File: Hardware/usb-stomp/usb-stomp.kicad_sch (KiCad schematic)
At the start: 30 parts, among them J1 Conn_01x12_MountingPin, J2 USB_C_Receptacle_USB2.0_16P, J3 BM28B0.6-24DS/2, J4 AudioJack4, J5 AudioJack4, J6 I2C1, SW1 SW_SPST, U1 TLV76733DRVx, U2 USBLC6-2P6, U3 74AHCT1G125, U4 TLP2310

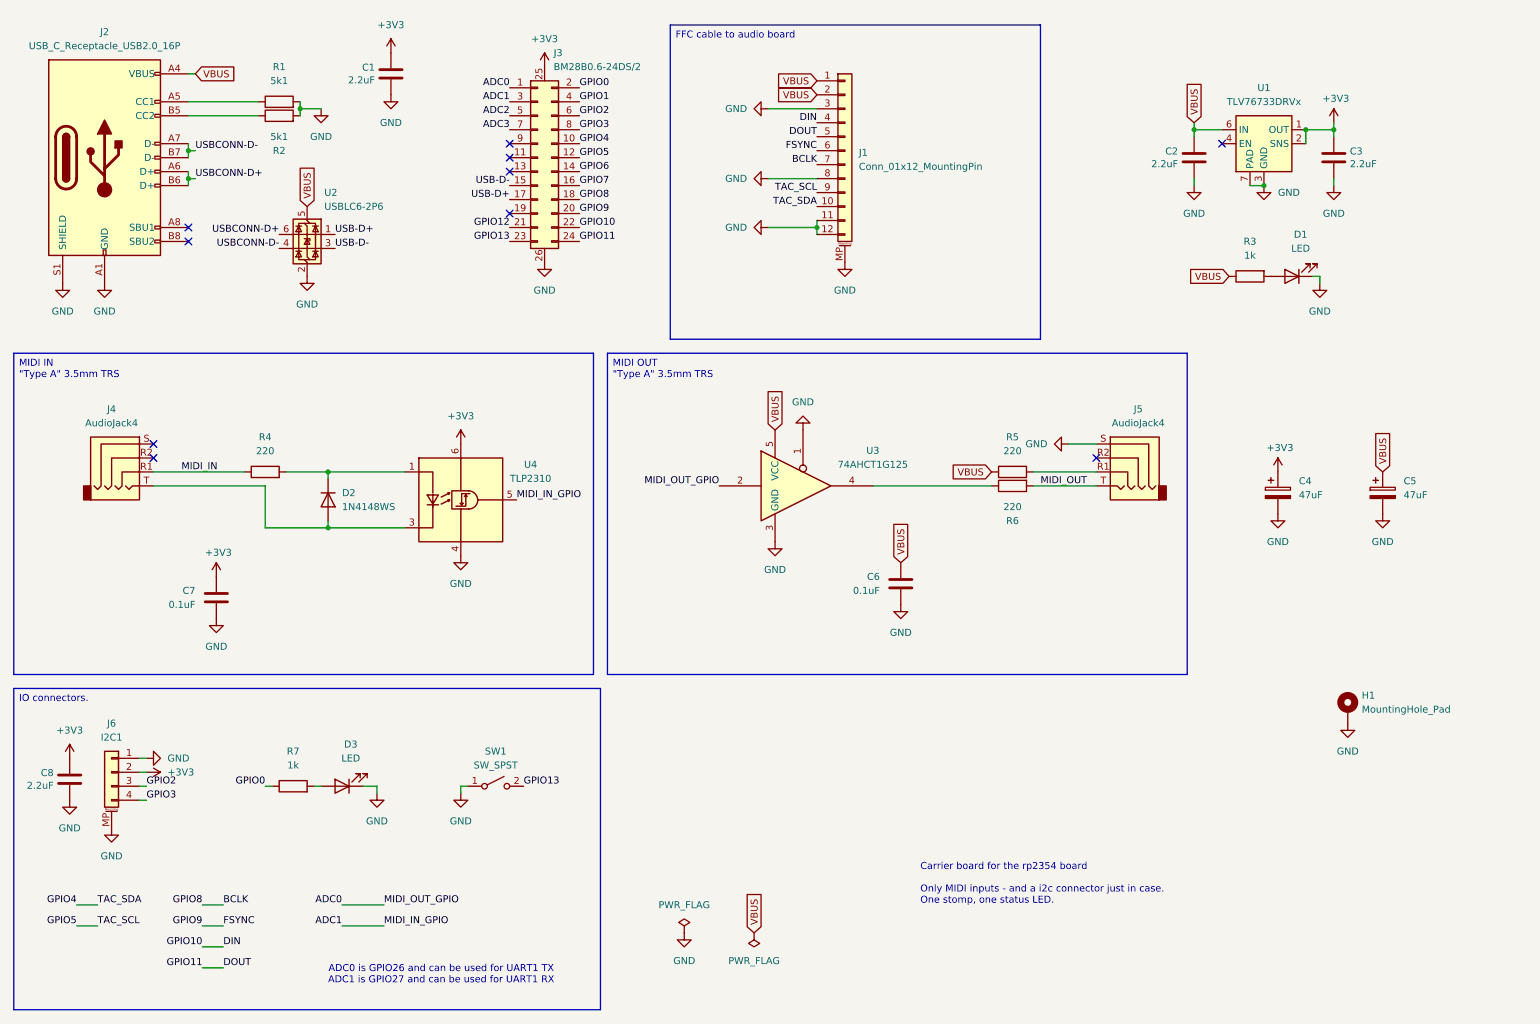
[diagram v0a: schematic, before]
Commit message: Update the "USB Stomp" board to use design blocks
This is pretty much a re-do of the "USB Stomp" board to include
everything into one single design and one single resulting board.

It makes little sense - it's not that interesting a board - but the
impetus was mostly just to learn and use new features, both on the
design side and on the manufacturing side.

So this does two very big things:

 - it uses the new TAC5242 / RP2354 design blocks as part of the
   schematic and the PCB layout.

 - the board is manufactured as one single flex board instead of having
   separate "audio jacks" and "USB stomp" boards

In other words, it's the same as the combination of the "audio jacks"
board and the previous "USB stomp" board, that used a FFC cable to
connect the two, except now the FFC cable is basically part of the
design, and the traditional rigid parts have been replaced by FR4
stiffeners instead.

In the process, this does various other minor changes:

 - No more separate BOOTSEL switch, which was a nightmare when the thing
   was boxed up. Instead, the stomp switch doubles up as the BOOTSEL
   switch too.

   Connecting the same switch to both a GPIO and BOOTSEL needs a bit of
   care: it would have been technically possible to only connect it to
   the the BOOTSEL pin, and read it that way with no GPIO at all, but
   the BOOTSEL line is also tied to the QSPI chip select pin, so then
   reading just the status requires turning off FLASH access.

   I considered doing exactly that, and it is entirely possible to do
   (micropython even has a "rp2.bootsel_button()" function for this),
   but when you use both cores, it's just very painful to make sure
   neither core is accessing the flash while you read the BOOTSEL
   status.

   So adding a little bit of hardware makes it much easier, and isolates
   the GPIO from the QSPI chip select using a dual diode. The switch
   pulls both low, but the wiggling of the QSPI CS line doesn't affect
   the GPIO.

   While at it, this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
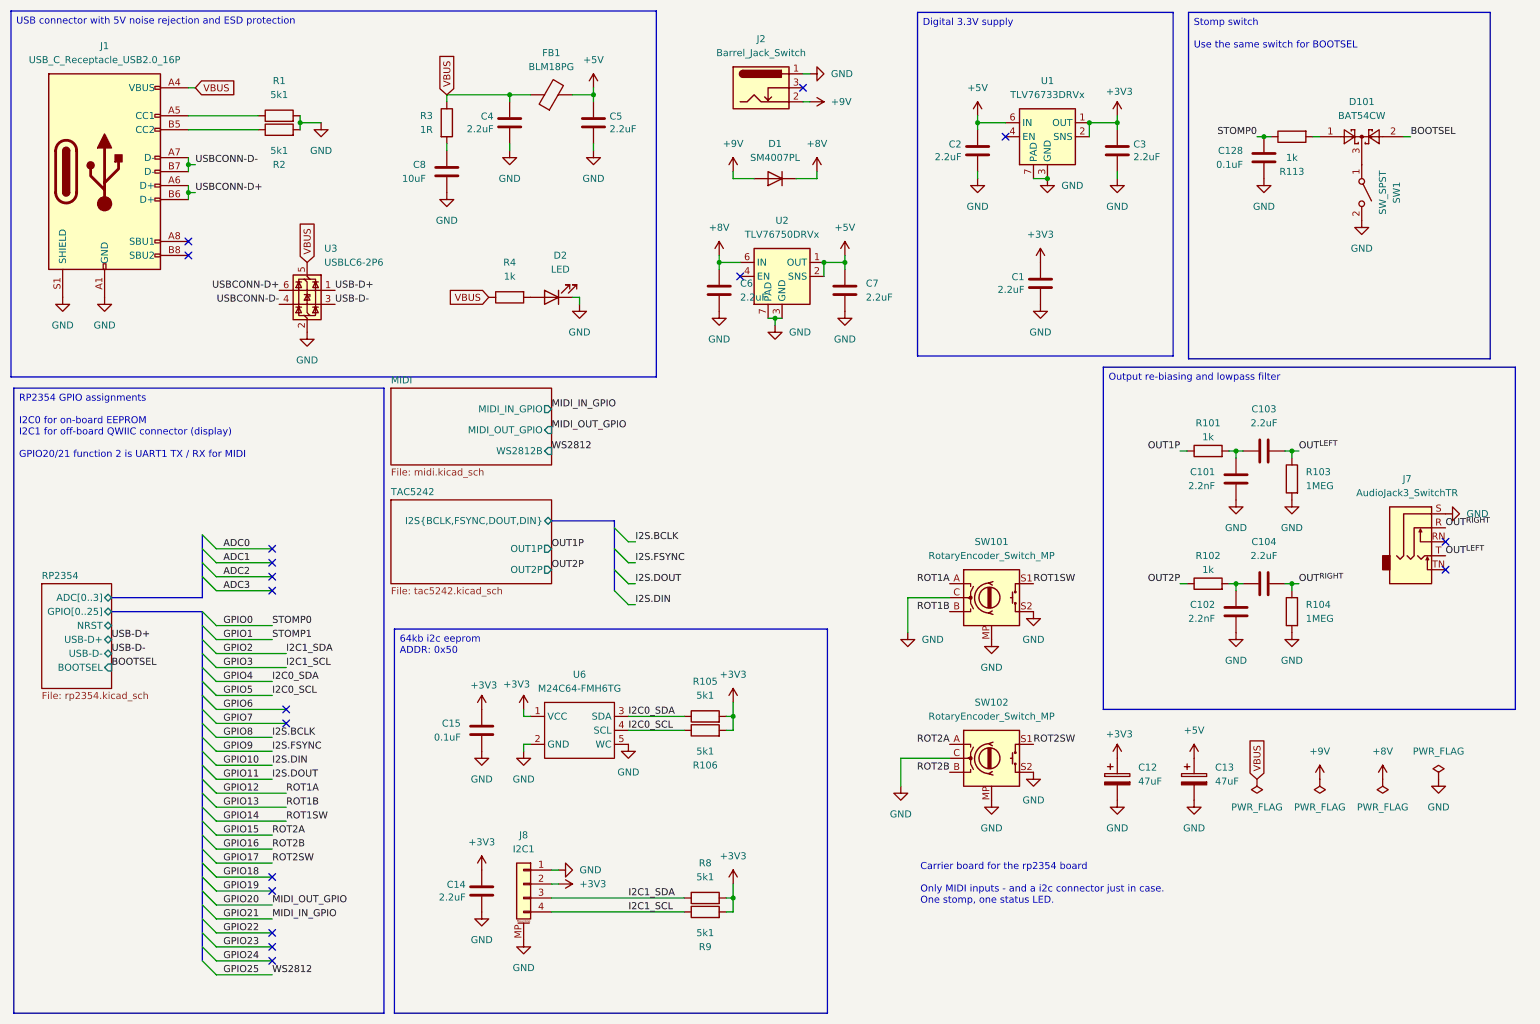
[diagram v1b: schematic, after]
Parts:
- removed D2: 1N4148WS, Diode_SMD:D_SOD-323, symbol Device:D
- removed D3: LED, LED_THT:LED_D5.0mm_FlatTop, symbol Device:LED
- removed H1: MountingHole_Pad, MountingHole:MountingHole_3.2mm_M3_DIN965_Pad, symbol Mechanical:MountingHole_Pad
- removed J1: Conn_01x12_MountingPin, Mylib:AFH-5-S12FIA-1H, symbol Connector_Generic_MountingPin:Conn_01x12_MountingPin
- removed J3: BM28B0.6-24DS/2, Mylib:BM28B0.6-24DS, symbol Mylib:BM28B0.6-24DS
- removed J4, J5: AudioJack4, Mylib:PJ-320D, symbol Connector_Audio:AudioJack4
- removed R4, R5, R6: 220, Resistor_SMD:R_0402_1005Metric, symbol Device:R
- removed R7: 1k, Resistor_SMD:R_0402_1005Metric, symbol Device:R
- removed U3: 74AHCT1G125, Package_TO_SOT_SMD:SOT-353_SC-70-5, symbol 74xGxx:74AHCT1G125
- removed U4: TLP2310, Package_SO:SO-5-6_4.55x3.7mm_P1.27mm, symbol Isolator:TLP2310
- added C101, C102: 2.2nF, Capacitor_SMD:C_0402_1005Metric, symbol Device:C
- added C103, C104, C4, C5: 2.2uF, Capacitor_SMD:C_0603_1608Metric, symbol Device:C
- added C128, C15: 0.1uF, Capacitor_SMD:C_0201_0603Metric, symbol Device:C
- added C8: 10uF, Capacitor_SMD:C_0603_1608Metric, symbol Device:C
- added D1: SM4007PL, Mylib:SOD-123FL, symbol Device:D
- added D101: BAT54CW, Package_TO_SOT_SMD:SOT-323_SC-70, symbol Diode:BAT54CW
- added FB1: BLM18PG, Inductor_SMD:L_0603_1608Metric, symbol Device:FerriteBead
- added J2: Barrel_Jack_Switch, Mylib:Wurth WR-DC 2.1mm Power Jack, symbol Connector:Barrel_Jack_Switch
- added J7: AudioJack3_SwitchTR, Mylib:NRJ6HM-1-PRE, symbol Connector_Audio:AudioJack3_SwitchTR
- added R101, R102, R113: 1k, Resistor_SMD:R_0402_1005Metric, symbol Device:R
- added R103, R104: 1MEG, Resistor_SMD:R_0402_1005Metric, symbol Device:R
- added R105, R106, R8, R9: 5k1, Resistor_SMD:R_0402_1005Metric, symbol Device:R
- added R3: 1R, Resistor_SMD:R_0402_1005Metric, symbol Device:R
- added SW101, SW102: RotaryEncoder_Switch_MP, Rotary_Encoder:RotaryEncoder_Alps_EC11E-Switch_Vertical_H20mm, symbol Device:RotaryEncoder_Switch_MP
- added U2: TLV76750DRVx, Package_SON:WSON-6-1EP_2x2mm_P0.65mm_EP1x1.6mm, symbol Regulator_Linear:TLV76750DRVx
- added U6: M24C64-FMH6TG, Mylib:UFDFPN5, symbol Mylib:M24C02-FMH
- C1, C2, C3: footprint Capacitor_SMD:C_0805_2012Metric -> Capacitor_SMD:C_0603_1608Metric; LCSC PN C77081 -> C415535
- C14: renamed from C8; footprint Capacitor_SMD:C_0805_2012Metric -> Capacitor_SMD:C_0603_1608Metric; LCSC PN C77081 -> C415535
- C6, C7: value 0.1uF -> 2.2uF; footprint Capacitor_SMD:C_0402_1005Metric -> Capacitor_SMD:C_0603_1608Metric; LCSC PN C1525 -> C415535
- R4: renamed from R3; LCSC PN C11702 -> C136974
- renumbered C4 to C12, C5 to C13, D1 to D2, J2 to J1, J6 to J8, U2 to U3
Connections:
- net +3V3: now also C15.1, R105.2, R106.2, R8.2, R9.2, U6.1 (VCC); no longer C7.2
- net GND: now also C6.2, C7.2, SW1.2 (B), C101.1, C102.1, C128.1, C15.2, C4.2, C5.2, C8.2, J2.1, J7.S, R103.2, R104.2, SW101.C, SW101.MP, SW101.S2, SW102.C, SW102.MP, SW102.S2, U2.3 (GND), U2.5 (GND), U2.7 (PAD), U6.2 (GND), U6.5 (WC); no longer C6.1, C7.1, SW1.1 (A)
- net GPIO0: now also C128.2, R113.1
- net GPIO12: now also SW101.A
- net GPIO13: now also SW101.B; no longer SW1.2 (B)
- net GPIO2: now also R8.1
- net GPIO3: now also R9.1
- net GPIO4: now also R105.1, U6.3 (SDA)
- net GPIO5: now also R106.1, U6.4 (SCL)
- net VBUS: now also C4.1, FB1.1, R3.1; no longer C13.1, C2.1, C6.2, U1.6 (IN)
- new net: C101.2, C103.1, R101.2
- new net: C102.2, C104.1, R102.2
- new net: D101.3, SW1.1 (A)
- new net: C8.1, R3.2
- new net: D101.1, R113.2
- new net +5V: C13.1, C2.1, C5.1, C7.1, FB1.2, U1.6 (IN), U2.1 (OUT), U2.2 (SNS)
- new net +8V: C6.1, D1.1 (K), U2.6 (IN)
- new net +9V: D1.2 (A), J2.2
- new net BOOTSEL: D101.2
- new net GPIO14: SW101.S1
- new net GPIO15: SW102.A
- new net GPIO16: SW102.B
- new net GPIO17: SW102.S1
- new net OUT1P: R101.1
- new net OUT2P: R102.1
- new net OUT^{LEFT}: C103.2, J7.T, R103.1
- new net OUT^{RIGHT}: C104.2, J7.R, R104.1
- no-connect marks 10 -> 18
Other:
- added sheet MIDI (midi.kicad_sch)
- added sheet RP2354 (rp2354.kicad_sch)
- added sheet TAC5242 (tac5242.kicad_sch)
- note removed: "ADC0 is GPIO26 and can be used for UART1 TX ADC1 is GPIO27 and can be used for UART1 RX"
- moved on the sheet: C1, C12, C13, C14, C2, C3, D2, J1, J8, R1, R2, R4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

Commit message: Let's re-do the usb-stomp board without the flex board
It was a teaching experience, but I guess the lesson was "don't do
that".  Let's just turn it into a straightforward simple single board.

I did decide to try a buck regulator, and I'm also playing with adding
support for a remote stomp switch or expression pedal.  I'm trying to do
it in a way that pretty much anything could be made to work - a single
remote stomp over a TS 1/4" cable, or a dual remote stomp over a TRS
one.  Or an expression pedal. But maybe I screwed that thing up.

The TRS Typa-A midi ports remain for remote control, but I'm thinking
that it shouldn't be too hard to teach WebMIDI to set up a model where
the remote stomp / expression pedal can control some arbitrary pot
value in the scene.

There's also a rotary encoder for the same reason - program the scene to
make it be the master volume, or the noise gate level, or whatever.

Of course, that "program the scene" part is all just a nebulous plan.  I
don't actually support that yet.  SMOP.

Signed-off-by: Linus Torvalds <torvalds@linux-foundation.org>
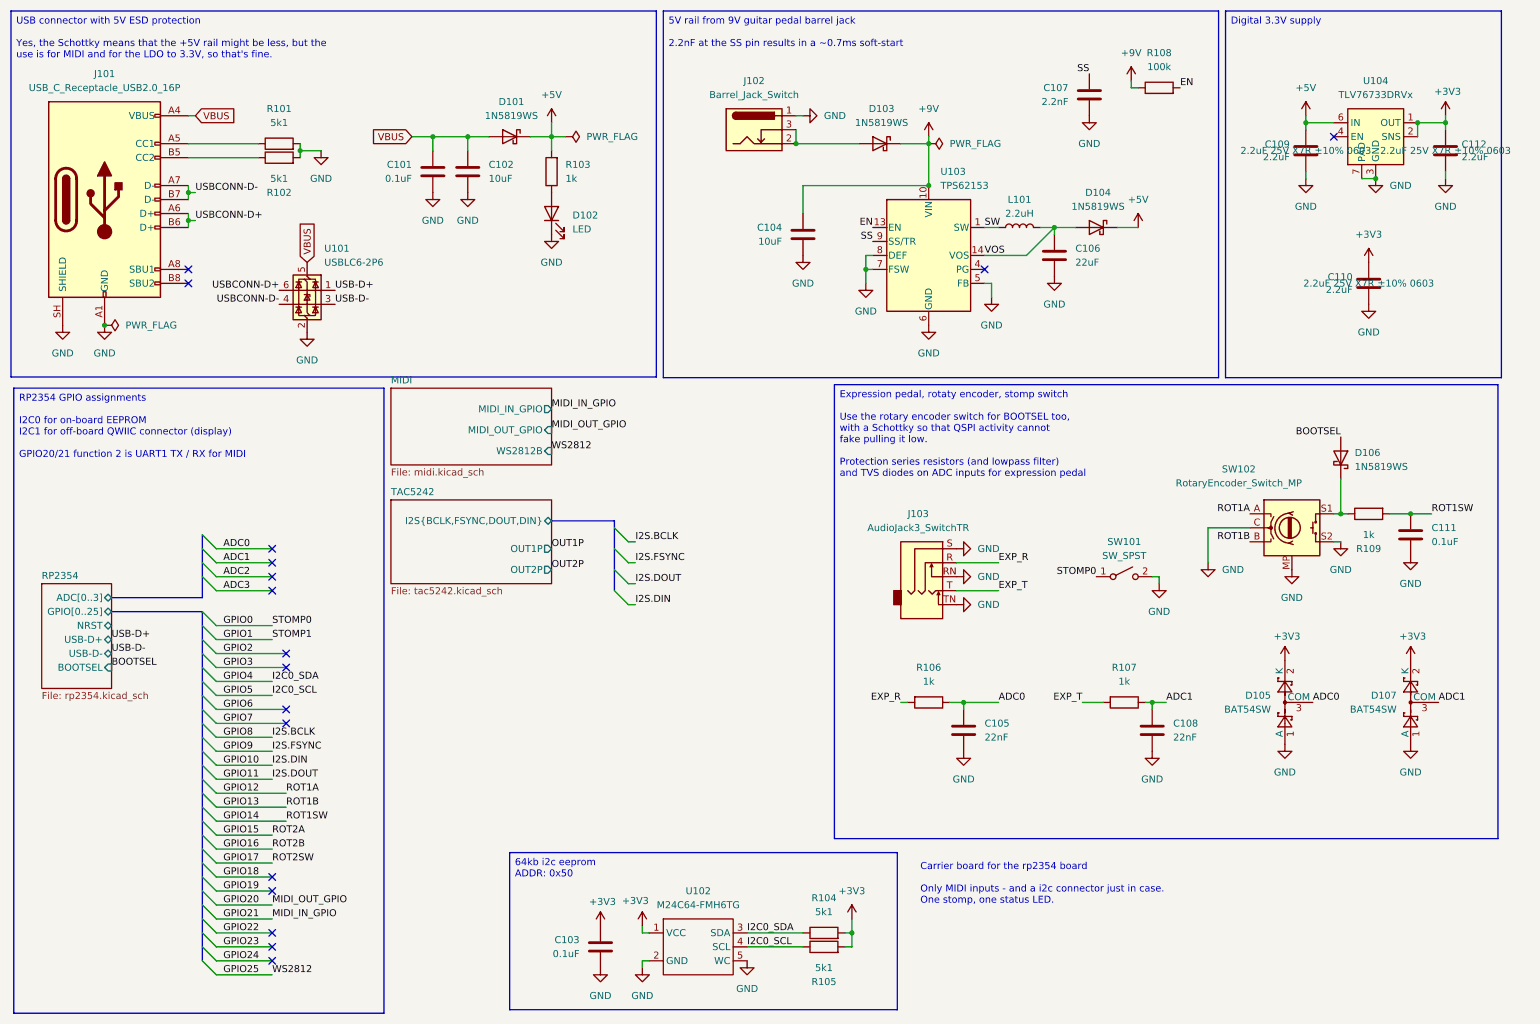
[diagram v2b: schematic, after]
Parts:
- removed C103, C14, C4, C5, C6, C7: 2.2uF, Capacitor_SMD:C_0603_1608Metric, symbol Device:C
- removed C12, C13: 47uF, Capacitor_SMD:CP_Elec_6.3x5.9, symbol Device:C_Polarized
- removed C8: 10uF, Capacitor_SMD:C_0603_1608Metric, symbol Device:C
- removed D1: SM4007PL, Mylib:SOD-123FL, symbol Device:D
- removed D101: BAT54CW, Package_TO_SOT_SMD:SOT-323_SC-70, symbol Diode:BAT54CW
- removed FB1: BLM18PG, Inductor_SMD:L_0603_1608Metric, symbol Device:FerriteBead
- removed J1: USB_C_Receptacle_USB2.0_16P, Connector_USB:USB_C_Receptacle_GCT_USB4105-xx-A_16P_TopMnt_Horizontal, symbol Connector:USB_C_Receptacle_USB2.0_16P
- removed J7: AudioJack3_SwitchTR, Mylib:NRJ6HM-1-PRE, symbol Connector_Audio:AudioJack3_SwitchTR
- removed J8: I2C1, Connector_JST:JST_SH_SM04B-SRSS-TB_1x04-1MP_P1.00mm_Horizontal, symbol Connector_Generic_MountingPin:Conn_01x04_MountingPin
- removed R101, R102: 1k, Resistor_SMD:R_0402_1005Metric, symbol Device:R
- removed R103, R104: 1MEG, Resistor_SMD:R_0402_1005Metric, symbol Device:R
- removed R3: 1R, Resistor_SMD:R_0402_1005Metric, symbol Device:R
- removed R8, R9: 5k1, Resistor_SMD:R_0402_1005Metric, symbol Device:R
- removed SW102: RotaryEncoder_Switch_MP, Rotary_Encoder:RotaryEncoder_Alps_EC11E-Switch_Vertical_H20mm, symbol Device:RotaryEncoder_Switch_MP
- removed U2: TLV76750DRVx, Package_SON:WSON-6-1EP_2x2mm_P0.65mm_EP1x1.6mm, symbol Regulator_Linear:TLV76750DRVx
- added C105, C108: 22nF, Capacitor_SMD:C_0402_1005Metric, symbol Device:C
- added C106: 22uF, Capacitor_SMD:C_1210_3225Metric, symbol Device:C
- added C107: 2.2nF, Capacitor_SMD:C_0402_1005Metric, symbol Device:C
- added D101, D103, D104, D106: 1N5819WS, Diode_SMD:D_SOD-323, symbol Device:D_Schottky
- added D105, D107: BAT54SW, Package_TO_SOT_SMD:SOT-323_SC-70, symbol Diode:BAT54SW
- added J101: USB_C_Receptacle_USB2.0_16P, Connector_USB:USB_C_Receptacle_GCT_USB4105-xx-A_16P_TopMnt_Horizontal, symbol Connector:USB_C_Receptacle_USB2.0_16P
- added J103: AudioJack3_SwitchTR, Mylib:NRJ6HM-1-PRE, symbol Connector_Audio:AudioJack3_SwitchTR
- added L101: 2.2uH, Mylib:L_0806, symbol Device:L
- added R106, R107: 1k, Resistor_SMD:R_0402_1005Metric, symbol Device:R
- added R108: 100k, Resistor_SMD:R_0402_1005Metric, symbol Device:R
- added U103: TPS62153, Package_DFN_QFN:VQFN-16-1EP_3x3mm_P0.5mm_EP1.68x1.68mm_ThermalVias, symbol Regulator_Switching:TPS62153
- C101: value 2.2nF -> 0.1uF; footprint Capacitor_SMD:C_0402_1005Metric -> Capacitor_SMD:C_0201_0603Metric; LCSC PN C2987940 -> C3901090; MANUFACTURER_PART_NUMBER GRM1555C1H222GA01D -> (none)
- C102: value 2.2nF -> 10uF; footprint Capacitor_SMD:C_0402_1005Metric -> Capacitor_SMD:C_0603_1608Metric; LCSC PN C2987940 -> C91606; MANUFACTURER_PART_NUMBER GRM1555C1H222GA01D -> (none)
- C104: value 2.2uF -> 10uF; LCSC PN C415535 -> C91606
- renumbered C15 to C103, C2 to C109, C1 to C110, C128 to C111, C3 to C112, D2 to D102, J2 to J102, R1 to R101, R2 to R102, R4 to R103, R105 to R104, R106 to R105, R113 to R109, SW1 to SW101, SW101 to SW102, U3 to U101, U6 to U102, U1 to U104
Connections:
- net OUT^{RIGHT} is gone; now on net GND: C104.2
- net +3V3: now also D105.2 (K), D107.2 (K)
- net +5V: now also R103.2, D101.1 (K), D104.1 (K)
- net +9V: now also C104.1, D103.1 (K), R108.1, U103.10 (VIN), U103.11 (VIN), U103.12 (VIN); no longer J102.2
- net ADC0: now also C105.1, D105.3 (COM), R106.1
- net ADC1: now also C108.1, D107.3 (COM), R107.1
- net BOOTSEL: now also D106.2 (A)
- net GND: now also C102.2, C105.2, C106.2, C107.1, C108.2, D105.1 (A), D107.1 (A), J101.A1 (GND), J101.A12 (GND), J101.B1 (GND), J101.B12 (GND), J101.SH (SHIELD), J103.RN, J103.S, J103.TN, U103.15 (GND), U103.16 (GND), U103.17 (GND), U103.5 (FB), U103.6 (GND), U103.7 (FSW), U103.8 (DEF); no longer C102.1
- net GPIO0: now also SW101.1 (A); no longer C111.2, R109.1
- net GPIO14: now also C111.2, R109.2; no longer SW102.S1
- net USBCONN-D+: now also J101.A6 (D+), J101.B6 (D+)
- net USBCONN-D-: now also J101.A7 (D-), J101.B7 (D-)
- net VBUS: now also C101.2, C102.1, D101.2 (A), J101.A4 (VBUS), J101.A9 (VBUS), J101.B4 (VBUS), J101.B9 (VBUS); no longer R103.1
- net at R101.1: now also J101.A5 (CC1)
- net at R102.1: now also J101.B5 (CC2)
- net at J102.3: now also J102.2, D103.2 (A)
- net at D102.2 (A): now also R103.1; no longer R103.2
- new net: D106.1 (K), R109.1, SW102.S1
- new net EN: R108.2, U103.13 (EN)
- new net EXP_R: J103.R, R106.2
- new net EXP_T: J103.T, R107.2
- new net SS: C107.2, U103.9 (SS/TR)
- new net SW: L101.1, U103.1 (SW), U103.2 (SW), U103.3 (SW)
- new net VOS: C106.1, D104.2 (A), L101.2, U103.14 (VOS)
- no-connect marks 18 -> 17
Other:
- moved on the sheet: C103, C109, C110, C111, C112, D102, J102, R101, R102, R103, R104, R105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
